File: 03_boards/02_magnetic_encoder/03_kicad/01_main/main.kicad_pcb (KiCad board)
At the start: 2 copper layers, 30 x 40 mm, 5 parts, among them J1 01x05, U1 AS5311-ATST-500

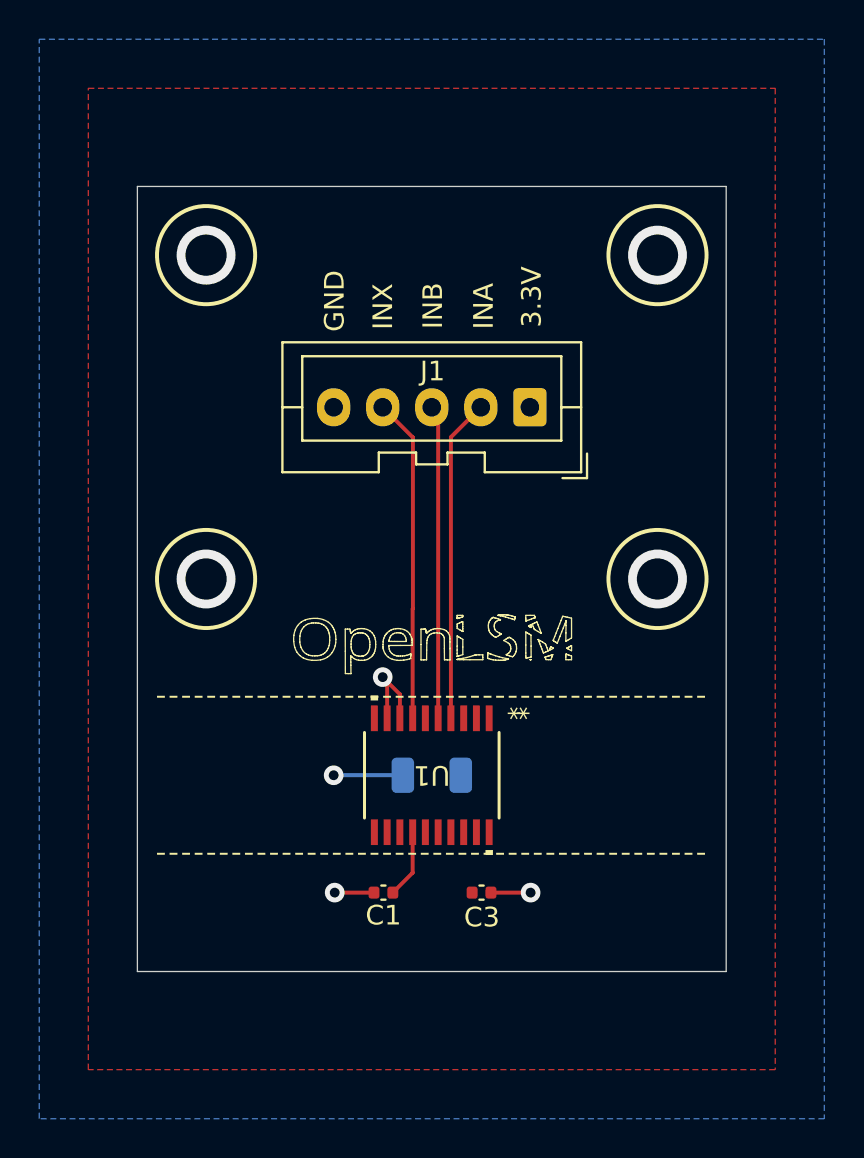
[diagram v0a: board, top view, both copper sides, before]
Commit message: Updated PCB for better mounting & also renamed reference in motor driver.
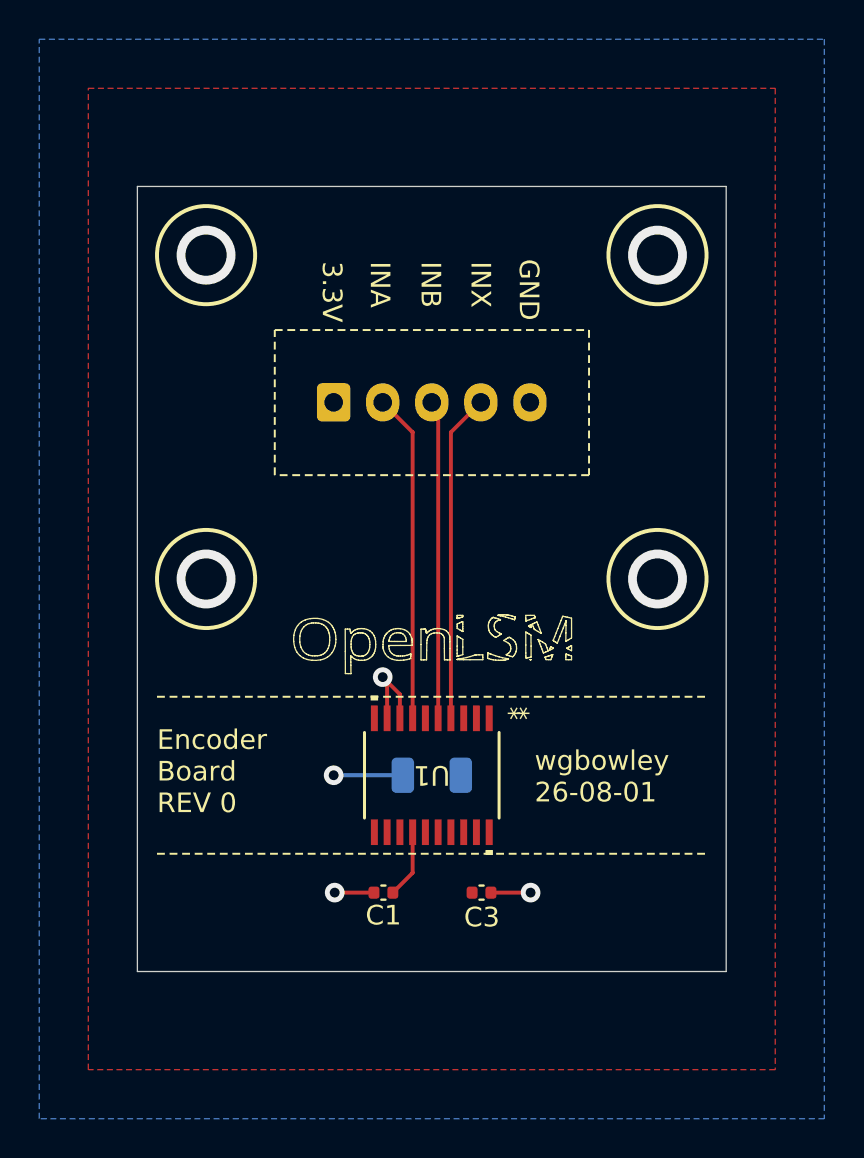
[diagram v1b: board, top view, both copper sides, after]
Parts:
- J1: moved to B.Cu
- moved J1 10.0 mm to (10.0, 11.0), turned to 0 degrees
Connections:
- J1 pad 2: INA -> INX
- J1 pad 4: INX -> INA
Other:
- board text added: "Encoder Board REV 0"
- board text added: "wgbowley 26-08-01"

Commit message: Improvement Mounting & Added note on CL
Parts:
- added R1: 0Ω, Resistor_SMD:R_0402_1005Metric, F.Cu at (10.0, 23.0)
- moved C2 13.5 mm to (15.0, 16.5)
- moved C1 12.2 mm to (10.0, 24.0)
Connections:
- C1 pad 1: GND -> Net-(U1-PROG)
- U1 pad 9: GND -> Net-(U1-PROG)
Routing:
- net Net-(U1-PROG): track 0.00 -> 5.04 mm
- net GND: track 12.2 -> 10.6 mm, vias 7 -> 8

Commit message: Updated Encoder KiCAD and removed actuation_comparsion
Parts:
- J1: footprint Connector_JST:JST_XA_B05B-XASK-1_1x05_P2.50mm_Vertical -> Connector_JST:JST_XH_B5B-XH-A_1x05_P2.50mm_Vertical
- U1: footprint AS5311:TSSOP20_AS5311-ATST-500_AMS -> footprints:TSSOP20_AS5311-ATST-500_AMS
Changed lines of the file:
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@@
 	)
 	(setup
+		(stackup
+			(layer "F.SilkS"
+				(type "Top Silk Screen")
+			)
+			(layer "F.Paste"
+				(type "Top Solder Paste")
+			)
+			(layer "F.Mask"
+				(type "Top Solder Mask")
+				(color "Black")
+				(thickness 0.01)
+			)
+			(layer "F.Cu"
+				(type "copper")
+				(thickness 0.035)
+			)
+			(layer "dielectric 1"
+				(type "core")
+				(thickness 1.51)
+				(material "FR4")
+				(epsilon_r 4.5)
+				(loss_tangent 0.02)
+			)
+			(layer "B.Cu"
+				(type "copper")
+				(thickness 0.035)
+			)
+			(layer "B.Mask"
+				(type "Bottom Solder Mask")
+				(color "Black")
+				(thickness 0.01)
+			)
+			(layer "B.Paste"
+				(type "Bottom Solder Paste")
+			)
+			(layer "B.SilkS"
+				(type "Bottom Silk Screen")
+			)
+			(copper_finish "None")
+			(dielectric_constraints no)
+		)
 		(pad_to_mask_clearance 0)
 		(allow_soldermask_bridges_in_footprints no)
@@
 		(capping no)
 		(filling no)
+		(zone_defaults)
 		(pcbplotparams
 			(layerselection 0x00000000_00000000_55555555_5755f5ff)
@@
 		)
 	)
-	(footprint "AS5311:TSSOP20_AS5311-ATST-500_AMS"
+	(footprint "footprints:TSSOP20_AS5311-ATST-500_AMS"
 		(layer "F.Cu")
 		(at 15 30 -90)
 		(tags "AS5311-ATST-500 ")
 		(property "Reference" "U1"
-			(at 0 0 0)
+			(at 0 0 270)
 			(unlocked yes)
 			(layer "F.SilkS")
@@
 		)
 		(property "Value" "AS5311-ATST-500"
-			(at -6.671061 0 180)
+			(at 0 0 270)
 			(unlocked yes)
 			(layer "F.Fab")
@@
 		)
 		(fp_text user "${REFERENCE}"
-			(at -5 0 180)
+			(at 0 0 270)
 			(unlocked yes)
 			(layer "F.Fab")
@@
 		)
 		(embedded_fonts no)
+		(model "C:/Users/WBowl/Documents/Work/OpenLSM/03_boards/02_magnetic_encoder/03_kicad/02_components/AS5311-ATST-500/20-pin_TSSOP_.step"
+			(offset
+				(xyz 0 0 0)
+			)
+			(scale
+				(xyz 1 1 1)
+			)
+			(rotate
+				(xyz 0 0 0)
+			)
+		)
 	)
 	(footprint "Capacitor_SMD:C_0402_1005Metric"
@@
 		)
 	)
-	(footprint "Connector_JST:JST_XA_B05B-XASK-1_1x05_P2.50mm_Vertical"
+	(footprint "Connector_JST:JST_XH_B5B-XH-A_1x05_P2.50mm_Vertical"
 		(layer "B.Cu")
 		(at 10 11)
-		(descr "JST XA series connector, B05B-XASK-1 (https://www.jst.com/wp-content/uploads/2021/01/eXA1.pdf)")
-		(tags "connector JST XA vertical")
+		(descr "JST XH series connector, B5B-XH-A (http://www.jst-mfg.com/product/pdf/eng/eXH.pdf)")
+		(tags "connector JST XH vertical")
 		(property "Reference" "J1"
-			(at 4.962319 -1.834061 0)
+			(at 5 3.55 180)
 			(layer "B.SilkS")
 			(effects
@@
 		)
 		(property "Value" "01x05"
-			(at -6.840413 0.45472 0)
+			(at 5 -4.6 180)
+			(layer "B.Fab")
+			(effects
+				(font
+					(size 1 1)
+					(thickness 0.15)
+				)
+				(justify mirror)
+			)
+		)
+		(property "Datasheet" ""
+			(at 0 0 180)
 			(layer "B.Fab")
 			(hide yes)
 			(effects
 				(font
-					(size 1 1)
-					(thickness 0.15)
+					(size 1.27 1.27)
 				)
 				(justify mirror)
 			)
 		)
-		(property "Datasheet" ""
-			(at 0 0 0)
+		(property "Description" "Generic connector, single row, 01x05, script generated (kicad-library-utils/schlib/autogen/connector/)"
+			(at 0 0 180)
 			(layer "B.Fab")
 			(hide yes)
@@
 			)
 		)
-		(property "Description" "Generic connector, single row, 01x05, script generated (kicad-library-utils/schlib/autogen/connector/)"
-			(at 0 0 0)
-			(layer "B.Fab")
-			(hide yes)
-			(effects
-				(font
-					(size 1.27 1.27)
-				)
-				(justify mirror)
-			)
-		)
 		(property "KiLib_Generator" "connector/JST"
-			(at 0 0 0)
+			(at 0 0 180)
 			(layer "B.SilkS")
 			(hide yes)
@@
 		(duplicate_pad_numbers_are_jumpers no)
 		(fp_line
-			(start -2.91 3.61)
-			(end -2.91 2.36)
+			(start -2.85 2.75)
+			(end -2.85 1.5)
 			(stroke
 				(width 0.12)
@@
 		)
 		(fp_line
-			(start -2.61 -3.31)
-			(end 12.61 -3.31)
+			(start -2.55 0.2)
+			(end -1.8 0.2)
 			(stroke
 				(width 0.12)
@@
 		)
 		(fp_line
-			(start -2.61 0)
-			(end -1.6 0)
+			(start -1.8 -2.75)
+			(end 5 -2.75)
 			(stroke
 				(width 0.12)
@@
 		)
 		(fp_line
-			(start -2.61 3.31)
-			(end -2.61 -3.31)
+			(start -1.8 0.2)
+			(end -1.8 -2.75)
 			(stroke
 				(width 0.12)
@@
 		)
 		(fp_line
-			(start -1.66 3.61)
-			(end -2.91 3.61)
+			(start -1.6 2.75)
+			(end -2.85 2.75)
 			(stroke
 				(width 0.12)
@@
 		)
 		(fp_line
-			(start -1.6 -2.6)
-			(end 11.6 -2.6)
+			(start 11.8 -2.75)
+			(end 5 -2.75)
 			(stroke
 				(width 0.12)
@@
 		)
 		(fp_line
-			(start -1.6 1.7)
-			(end -1.6 -2.6)
+			(start 11.8 0.2)
+			(end 11.8 -2.75)
 			(stroke
 				(width 0.12)
@@
 		)
 		(fp_line
-			(start 2.3 2.31)
-			(end 2.3 3.31)
+			(start 12.55 0.2)
+			(end 11.8 0.2)
 			(stroke
 				(width 0.12)
@@
 			(layer "B.SilkS")
 		)
-		(fp_line
-			(start 2.3 3.31)
-			(end -2.61 3.31)
+		(fp_rect
+			(start -2.56 2.46)
+			(end 12.56 -3.51)
 			(stroke
 				(width 0.12)
 				(type solid)
 			)
+			(fill no)
 			(layer "B.SilkS")
 		)
-		(fp_line
-			(start 4.2 2.31)
-			(end 2.3 2.31)
+		(fp_rect
+			(start -2.55 2.45)
+			(end -0.75 1.7)
 			(stroke
 				(width 0.12)
 				(type solid)
 			)
+			(fill no)
 			(layer "B.SilkS")
 		)
-		(fp_line
-			(start 4.2 2.91)
-			(end 4.2 2.31)
+		(fp_rect
+			(start 0.75 2.45)
+			(end 9.25 1.7)
 			(stroke
 				(width 0.12)
 				(type solid)
 			)
+			(fill no)
 			(layer "B.SilkS")
 		)
-		(fp_line
-			(start 5.8 2.31)
-			(end 5.8 2.91)
+		(fp_rect
+			(start 10.75 2.45)
+			(end 12.55 1.7)
 			(stroke
 				(width 0.12)
 				(type solid)
 			)
+			(fill no)
 			(layer "B.SilkS")
 		)
-		(fp_line
-			(start 5.8 2.91)
-			(end 4.2 2.91)
-			(stroke
-				(width 0.12)
-				(type solid)
-			)
-			(layer "B.SilkS")
-		)
-		(fp_line
-			(start 7.7 2.31)
-			(end 5.8 2.31)
-			(stroke
-				(width 0.12)
-				(type solid)
-			)
-			(layer "B.SilkS")
-		)
-		(fp_line
-			(start 7.7 3.31)
-			(end 7.7 2.31)
-			(stroke
-				(width 0.12)
-				(type solid)
-			)
-			(layer "B.SilkS")
-		)
-		(fp_line
-			(start 11.6 -2.6)
-			(end 11.6 1.7)
-			(stroke
-				(width 0.12)
-				(type solid)
-			)
-			(layer "B.SilkS")
-		)
-		(fp_line
-			(start 11.6 1.7)
-			(end -1.6 1.7)
-			(stroke
-				(width 0.12)
-				(type solid)
-			)
-			(layer "B.SilkS")
-		)
-		(fp_line
-			(start 12.61 -3.31)
-			(end 12.61 3.31)
-			(stroke
-				(width 0.12)
-				(type solid)
-			)
-			(layer "B.SilkS")
-		)
-		(fp_line
-			(start 12.61 0)
-			(end 11.6 0)
-			(stroke
-				(width 0.12)
-				(type solid)
-			)
-			(layer "B.SilkS")
-		)
-		(fp_line
-			(start 12.61 3.31)
-			(end 7.7 3.31)
-			(stroke
-				(width 0.12)
-				(type solid)
-			)
-			(layer "B.SilkS")
-		)
 		(fp_rect
-			(start -3 3.7)
-			(end 13 -3.7)
+			(start -2.95 2.85)
+			(end 12.95 -3.9)
 			(stroke
 				(width 0.05)
@@
 		)
 		(fp_line
-			(start -2.91 3.61)
-			(end -2.91 2.36)
+			(start -0.625 2.35)
+			(end 0 1.35)
 			(stroke
 				(width 0.1)
@@
 		)
 		(fp_line
-			(start -1.66 3.61)
-			(end -2.91 3.61)
+			(start 0 1.35)
+			(end 0.625 2.35)
 			(stroke
 				(width 0.1)
@@
 		)
 		(fp_rect
-			(start -2.5 3.2)
-			(end 12.5 -3.2)
+			(start -2.45 2.35)
+			(end 12.45 -3.4)
 			(stroke
 				(width 0.1)
@@
 		)
 		(fp_text user "${REFERENCE}"
-			(at 5 -2 0)
+			(at 5 -2.7 180)
 			(layer "B.Fab")
 			(effects
@@
 		)
 		(embedded_fonts no)
-		(model "${KICAD10_3DMODEL_DIR}/Connector_JST.3dshapes/JST_XA_B05B-XASK-1_1x05_P2.50mm_Vertical.step"
+		(model "${KICAD10_3DMODEL_DIR}/Connector_JST.3dshapes/JST_XH_B5B-XH-A_1x05_P2.50mm_Vertical.step"
 			(offset
 				(xyz 0 0 0)
